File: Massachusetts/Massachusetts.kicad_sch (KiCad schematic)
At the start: 12 parts, among them SW1 SW_Push

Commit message: linked schematic symbols to footprints
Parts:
- D1: footprint (none) -> LED_SMD:LED_0402_1005Metric_Pad0.77x0.64mm_HandSolder
- D2, D3, D4, D5: footprint (none) -> LED_SMD:LED_0201_0603Metric_Pad0.64x0.40mm_HandSolder
- R1, R2, R3, R4, R5: footprint (none) -> Resistor_SMD:R_01005_0402Metric_Pad0.57x0.30mm_HandSolder
- SW1: footprint (none) -> Button_Switch_THT:SW_PUSH_6mm_H4.3mm
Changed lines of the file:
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@@
 			)
 		)
-		(property "Footprint" ""
+		(property "Footprint" "Resistor_SMD:R_01005_0402Metric_Pad0.57x0.30mm_HandSolder"
 			(at 71.12 56.388 90)
 			(effects
@@
 			)
 		)
-		(property "Footprint" ""
+		(property "Footprint" "LED_SMD:LED_0201_0603Metric_Pad0.64x0.40mm_HandSolder"
 			(at 86.36 26.67 0)
 			(effects
@@
 			)
 		)
-		(property "Footprint" ""
+		(property "Footprint" "Resistor_SMD:R_01005_0402Metric_Pad0.57x0.30mm_HandSolder"
 			(at 71.12 79.248 90)
 			(effects
@@
 			)
 		)
-		(property "Footprint" ""
+		(property "Footprint" "LED_SMD:LED_0402_1005Metric_Pad0.77x0.64mm_HandSolder"
 			(at 86.36 67.31 0)
 			(effects
@@
 			)
 		)
-		(property "Footprint" ""
+		(property "Footprint" "LED_SMD:LED_0201_0603Metric_Pad0.64x0.40mm_HandSolder"
 			(at 86.36 54.61 0)
 			(effects
@@
 			)
 		)
-		(property "Footprint" ""
+		(property "Footprint" "LED_SMD:LED_0201_0603Metric_Pad0.64x0.40mm_HandSolder"
 			(at 86.36 39.37 0)
 			(effects
@@
 			)
 		)
-		(property "Footprint" ""
+		(property "Footprint" "Button_Switch_THT:SW_PUSH_6mm_H4.3mm"
 			(at 34.29 86.36 0)
 			(effects
@@
 			)
 		)
-		(property "Footprint" ""
+		(property "Footprint" "LED_SMD:LED_0201_0603Metric_Pad0.64x0.40mm_HandSolder"
 			(at 86.36 77.47 0)
 			(effects
@@
 			)
 		)
-		(property "Footprint" ""
+		(property "Footprint" "Resistor_SMD:R_01005_0402Metric_Pad0.57x0.30mm_HandSolder"
 			(at 71.12 28.448 90)
 			(effects
@@
 			)
 		)
-		(property "Footprint" ""
+		(property "Footprint" "Resistor_SMD:R_01005_0402Metric_Pad0.57x0.30mm_HandSolder"
 			(at 71.12 41.148 90)
 			(effects
@@
 			)
 		)
-		(property "Footprint" ""
+		(property "Footprint" "Resistor_SMD:R_01005_0402Metric_Pad0.57x0.30mm_HandSolder"
 			(at 71.12 69.088 90)
 			(effects

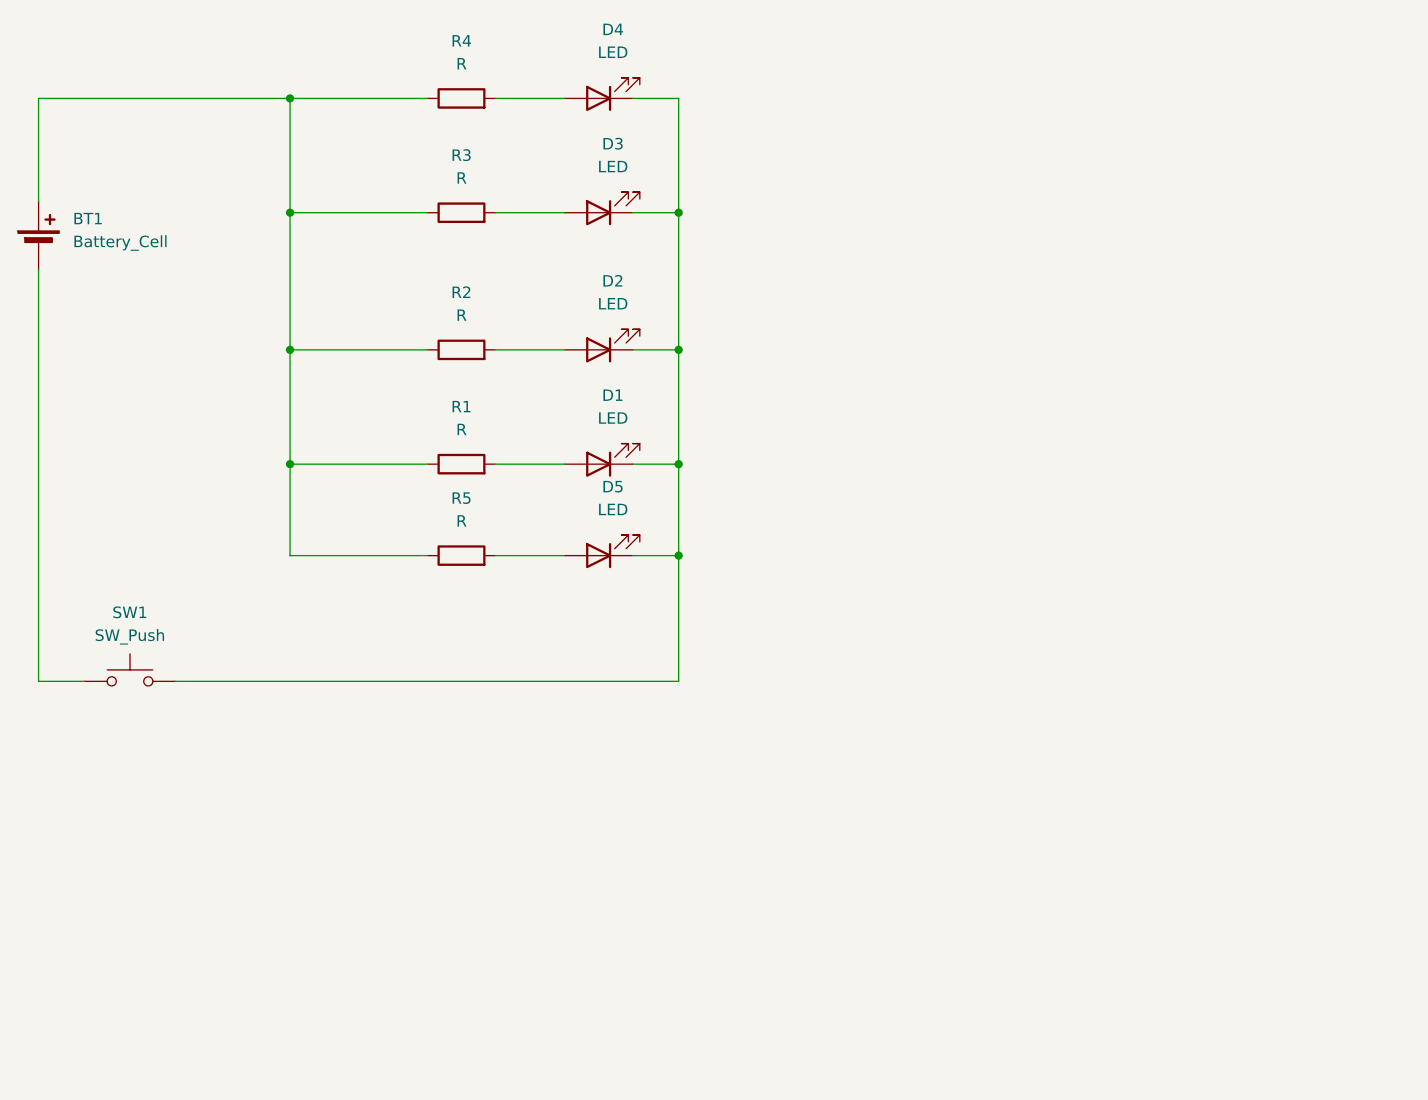
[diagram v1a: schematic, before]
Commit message: Added touch slider
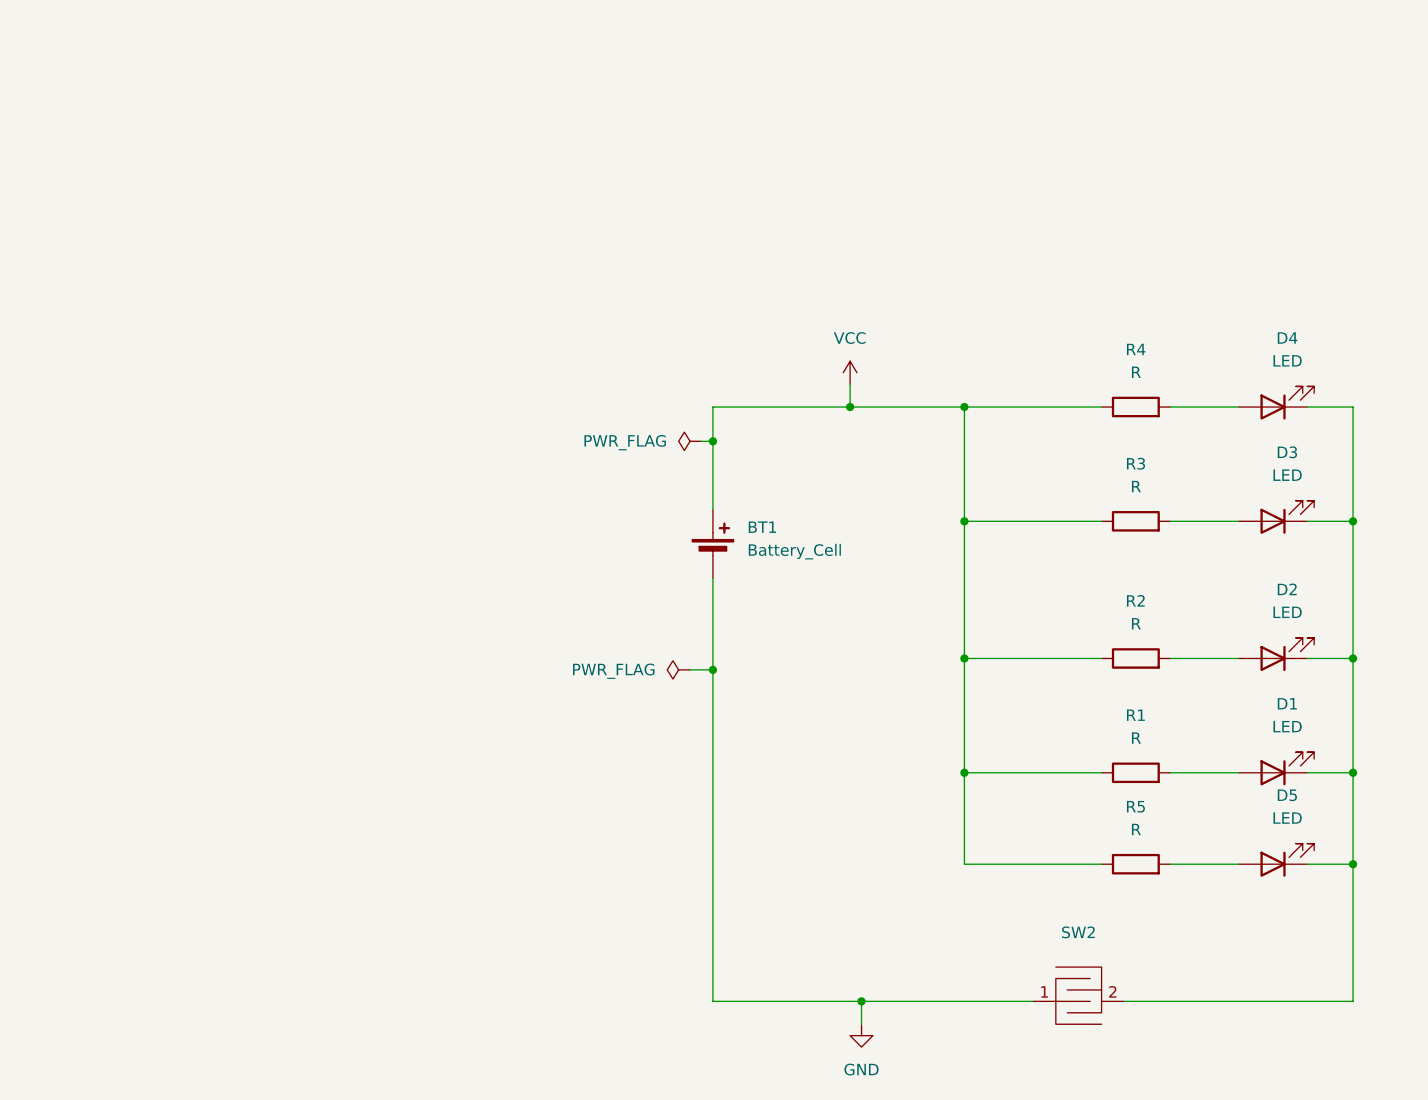
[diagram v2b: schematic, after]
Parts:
- removed SW1: SW_Push, Button_Switch_THT:SW_PUSH_6mm_H4.3mm, symbol Switch:SW_Push
- added SW2: ~, touchswitch:Touch_Switch, symbol touchswitch:Touch_Switch
- BT1: footprint Battery:BatteryHolder_Keystone_2466_1xAAA -> Battery:BatteryHolder_Keystone_3034_1x20mm
- D1: footprint LED_SMD:LED_0402_1005Metric_Pad0.77x0.64mm_HandSolder -> LED_SMD:LED_0603_1608Metric_Pad1.05x0.95mm_HandSolder
- D2, D3, D4, D5: footprint LED_SMD:LED_0201_0603Metric_Pad0.64x0.40mm_HandSolder -> LED_SMD:LED_0603_1608Metric_Pad1.05x0.95mm_HandSolder
- R1, R2, R3, R4, R5: footprint Resistor_SMD:R_01005_0402Metric_Pad0.57x0.30mm_HandSolder -> Resistor_SMD:R_0603_1608Metric_Pad0.98x0.95mm_HandSolder
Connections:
- net VCC: now reaches BT1.1 (+), R1.1, R2.1, R3.1, R4.1, R5.1
- net at D1.1 (K), D2.1 (K), D3.1 (K)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: now also SW2.2 (B)
- net GND: now reaches BT1.2 (-)
- net GND: now also SW2.1 (A)
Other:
- company: (none) -> Scarab Tech LLC
- title: (none) -> Mass
- moved on the sheet: BT1, D1, D2, D3, D4, D5, R1, R2, R3, R4, R5

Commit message: V1 ordered
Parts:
- removed SW2: ~, touchswitch:Touch_Switch, symbol touchswitch:Touch_Switch
- added S1: TL3315NF160Q, TL3315NF160Q:SW_TL3315NF160Q, symbol TL3315NF160Q:TL3315NF160Q
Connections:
- net GND: now also S1.1, S1.2
- net at D1.1 (K), D2.1 (K), D3.1 (K)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: now also S1.3, S1.4
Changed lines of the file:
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@@
+	)
+	(junction
+		(at 115.57 127)
+		(diameter 0)
+		(color 0 0 0 0)
 	)
 	(junction
@@
 	)
 	(junction
-		(at 115.57 127)
-		(diameter 0)
-		(color 0 0 0 0)
-	)
-	(junction
 		(at 127 88.9)
 		(diameter 0)
@@
 	(wire
 		(pts
-			(xy 115.57 127) (xy 115.57 129.54)
-		)
-		(stroke
-			(width 0)
-			(type default)
-		)
-	)
-	(wire
-		(pts
 			(xy 114.3 60.96) (xy 127 60.96)
 		)
@@
 	(wire
 		(pts
-			(xy 170.18 127) (xy 144.78 127)
-		)
-		(stroke
-			(width 0)
-			(type default)
-		)
-	)
-	(wire
-		(pts
 			(xy 149.86 111.76) (xy 157.48 111.76)
 		)
@@
 	(wire
 		(pts
+			(xy 115.57 129.54) (xy 115.57 127)
+		)
+		(stroke
+			(width 0)
+			(type default)
+		)
+	)
+	(wire
+		(pts
 			(xy 149.86 101.6) (xy 157.48 101.6)
 		)
@@
 	(wire
 		(pts
-			(xy 115.57 127) (xy 134.62 127)
+			(xy 115.57 127) (xy 132.08 127)
 		)
 		(stroke
@@
 	(wire
 		(pts
-			(xy 170.18 111.76) (xy 170.18 127)
+			(xy 176.53 111.76) (xy 176.53 127)
 		)
 		(stroke
@@
 	(wire
 		(pts
+			(xy 147.32 127) (xy 176.53 127)
+		)
+		(stroke
+			(width 0)
+			(type default)
+		)
+	)
+	(wire
+		(pts
 			(xy 99.06 127) (xy 115.57 127)
 		)
@@
 	(wire
 		(pts
+			(xy 176.53 111.76) (xy 170.18 111.76)
+		)
+		(stroke
+			(width 0)
+			(type default)
+		)
+	)
+	(wire
+		(pts
 			(xy 170.18 73.66) (xy 165.1 73.66)
 		)
@@
 			(width 0)
 			(type default)
-		)
-	)
-	(symbol
-		(lib_name "Touch_Switch_1")
-		(lib_id "touchswitch:Touch_Switch")
-		(at 139.7 127 0)
-		(unit 1)
-		(exclude_from_sim no)
-		(in_bom yes)
-		(on_board yes)
-		(dnp no)
-		(fields_autoplaced yes)
-		(property "Reference" "SW2"
-			(at 139.7 119.38 0)
-			(effects
-				(font
-					(size 1.27 1.27)
-				)
-			)
-		)
-		(property "Value" "~"
-			(at 139.7 121.92 0)
-			(effects
-				(font
-					(size 1.27 1.27)
-				)
-			)
-		)
-		(property "Footprint" "touchswitch:Touch_Switch"
-			(at 139.7 127 0)
-			(effects
-				(font
-					(size 1.27 1.27)
-				)
-				(hide yes)
-			)
-		)
-		(property "Datasheet" ""
-			(at 139.7 127 0)
-			(effects
-				(font
-					(size 1.27 1.27)
-				)
-				(hide yes)
-			)
-		)
-		(property "Description" ""
-			(at 139.7 127 0)
-			(effects
-				(font
-					(size 1.27 1.27)
-				)
-				(hide yes)
-			)
-		)
-		(pin "1"
-		)
-		(pin "2"
-		)
-		(instances
-			(project ""
-				(path "/ffc31004-9a37-4564-807a-8d2e1bc24eb6"
-					(reference "SW2")
-					(unit 1)
-				)
-			)
 		)
 	)
@@
 					(unit 1)
 				)
+			)
+		)
+	)
+	(symbol
+		(lib_id "TL3315NF160Q:TL3315NF160Q")
+		(at 139.7 127 0)
+		(unit 1)
+		(exclude_from_sim no)
+		(in_bom yes)
+		(on_board yes)
+		(dnp no)
+		(fields_autoplaced yes)
+		(property "Reference" "S1"
+			(at 139.7 118.11 0)
+			(effects
+				(font
+					(size 1.27 1.27)
+				)
+			)
+		)
+		(property "Value" "TL3315NF160Q"
+			(at 139.7 120.65 0)
+			(effects
+				(font
+					(size 1.27 1.27)
+				)
+			)
+		)
+		(property "Footprint" "TL3315NF160Q:SW_TL3315NF160Q"
+			(at 139.7 127 0)
+			(effects
+				(font
+					(size 1.27 1.27)
+				)
+				(justify bottom)
+				(hide yes)
+			)
+		)
+		(property "Datasheet" ""
+			(at 139.7 127 0)
+			(effects
+				(font
+					(size 1.27 1.27)
+				)
+				(hide yes)
+			)
+		)
+		(property "Description" ""
+			(at 139.7 127 0)
+			(effects
+				(font
+					(size 1.27 1.27)
+				)
+				(hide yes)
+			)
+		)
+		(property "PARTREV" "B"
+			(at 139.7 127 0)
+			(effects
+				(font
+					(size 1.27 1.27)
+				)
+				(justify bottom)
+				(hide yes)
+			)
+		)
+		(property "STANDARD" "Manufacturer recommendations"
+			(at 139.7 127 0)
+			(effects
+				(font
+					(size 1.27 1.27)
+				)
+				(justify bottom)
+				(hide yes)
+			)
+		)
+		(property "MAXIMUM_PACKAGE_HEIGHT" "0.8mm"
+			(at 139.7 127 0)
+			(effects
+				(font
+					(size 1.27 1.27)
+				)
+				(justify bottom)
+				(hide yes)
+			)
+		)
+		(property "MANUFACTURER" "E-Switch"
+			(at 139.7 127 0)
+			(effects
+				(font
+					(size 1.27 1.27)
+				)
+				(justify bottom)
+				(hide yes)
+			)
+		)
+		(pin "1"
+		)
+		(pin "4"
+		)
+		(pin "2"
+		)
+		(pin "3"
+		)
+		(instances
+			(project ""
+				(path "/ffc31004-9a37-4564-807a-8d2e1bc24eb6"
+					(reference "S1")
+					(unit 1)
+				)
